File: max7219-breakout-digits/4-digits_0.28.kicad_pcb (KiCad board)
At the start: 2 copper layers, 51 x 12 mm, 6 parts, among them J1 Conn_02x08_Odd_Even, U1 HDSM-443B_CC_2Digit_7Segment_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, U2 HDSM-443B_CC_2Digit_7Segment_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

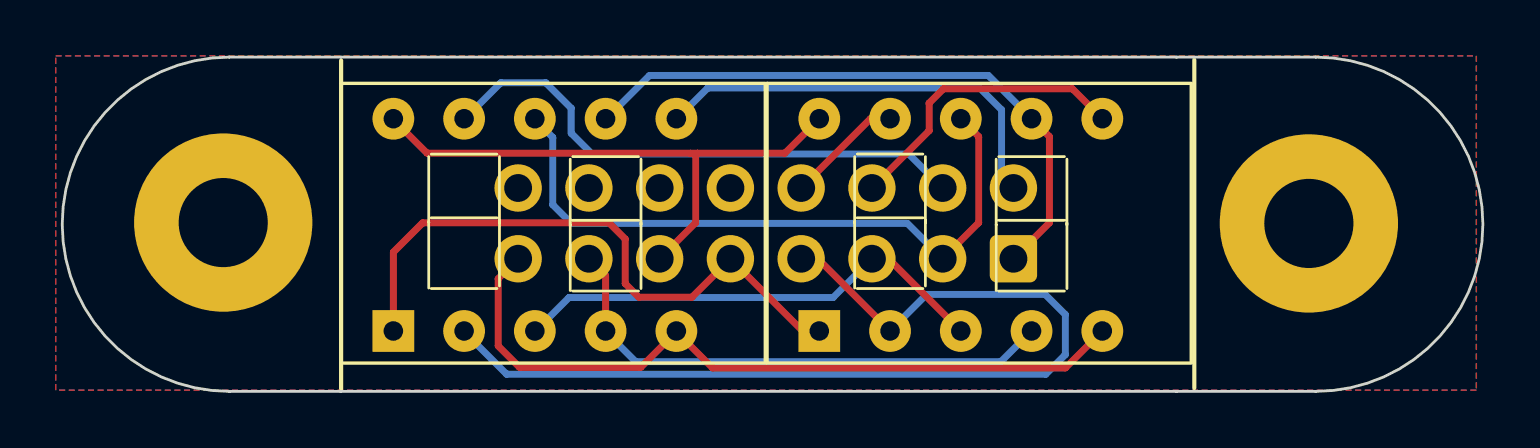
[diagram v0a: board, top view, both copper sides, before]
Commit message: rotate IDC on 0.28 displays, plated mounting holes for 0.35 displays, set version for 0.35 displays
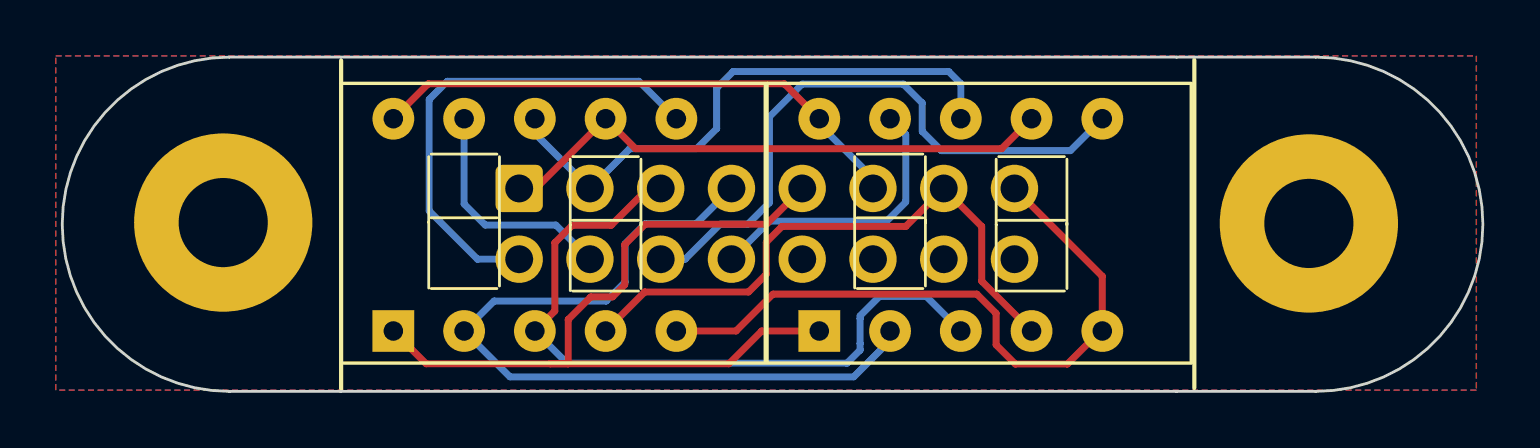
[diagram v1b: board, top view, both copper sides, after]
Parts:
- moved J1 17.9 mm to (87.0, 58.3), turned to -90 degrees
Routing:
- net /DIG2: track 10.8 -> 22.3 mm
- net /DIG1: track 19.8 -> 8.40 mm
- net /C: track 18.5 -> 26.1 mm
- net /E: track 22.3 -> 29.7 mm
- net /DIG3: track 4.22 -> 10.3 mm
- net /D: track 35.3 -> 29.4 mm
- net /B: track 24.0 -> 20.7 mm
- net /DP: track 27.1 -> 24.5 mm
- net /A: track 22.9 -> 20.3 mm
- net /DIG0: track 15.9 -> 17.6 mm
- net /G: track 19.6 -> 21.4 mm

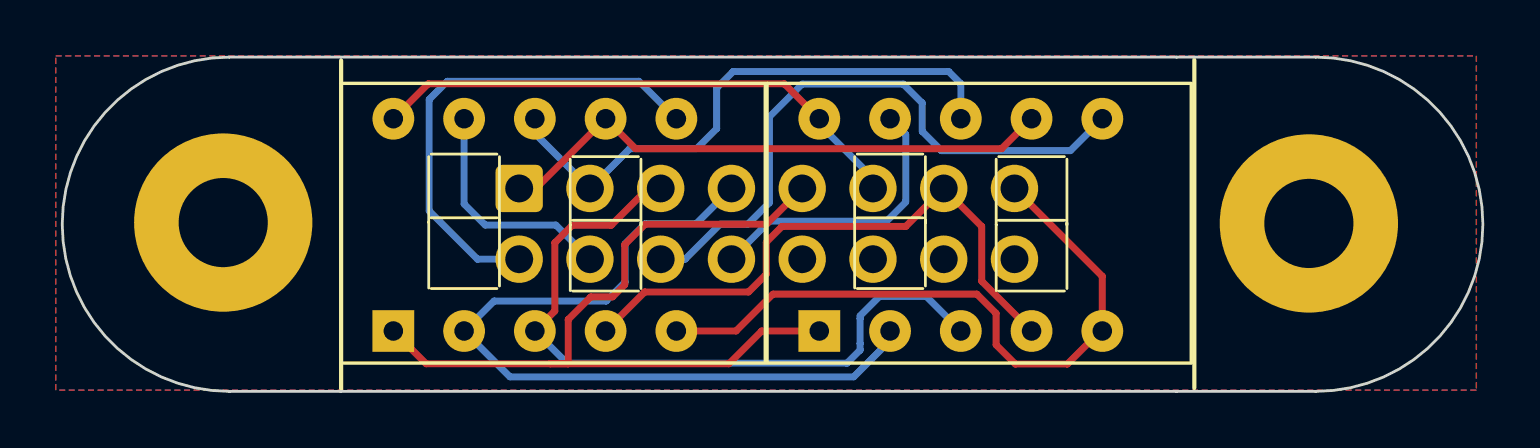
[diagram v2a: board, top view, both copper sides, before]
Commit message: add additional labels on front on backside from all boards
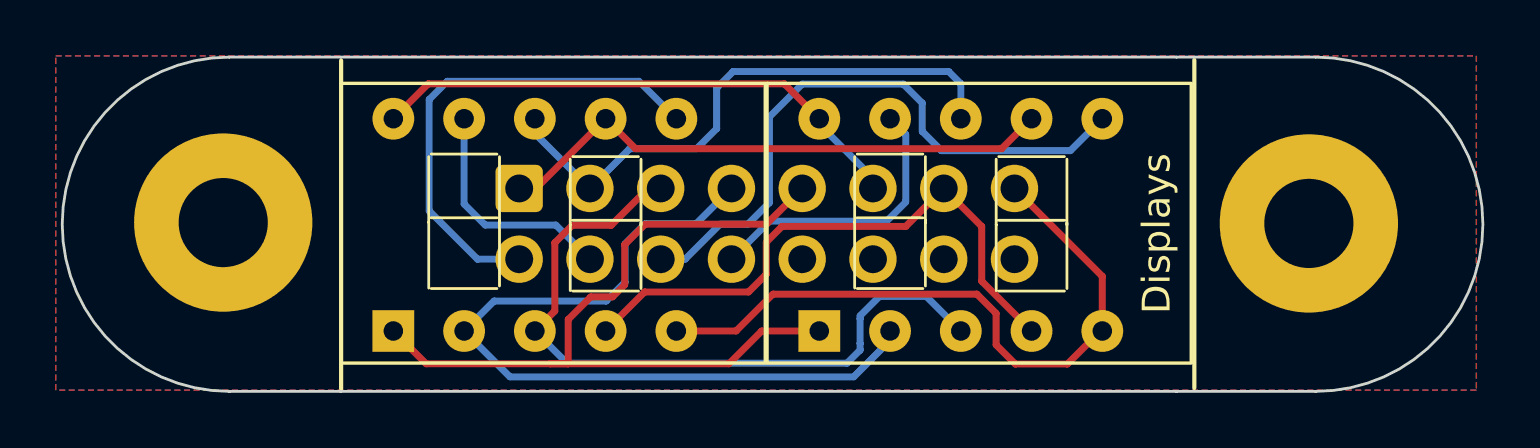
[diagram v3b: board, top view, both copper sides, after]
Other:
- board text added: "Displays"
- board text added: "IDC"
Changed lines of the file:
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@@
 		(layer "Edge.Cuts")
+	)
+	(gr_text "Displays"
+		(at 110.49 62.851449 90)
+		(layer "F.SilkS" knockout)
+		(effects
+			(font
+				(size 1 1)
+				(thickness 0.15)
+			)
+			(justify left bottom)
+		)
 	)
 	(gr_text "MobiFlight Display System 4 Digits ${REVISION}"
@@
 		)
 	)
+	(gr_text "IDC"
+		(at 84.52 56.98002 90)
+		(layer "B.SilkS" knockout)
+		(effects
+			(font
+				(size 2 2)
+				(thickness 0.25)
+			)
+			(justify left bottom mirror)
+		)
+	)
